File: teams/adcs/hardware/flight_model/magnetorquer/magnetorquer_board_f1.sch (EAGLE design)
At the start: 35 parts, among them U5 LTC3624

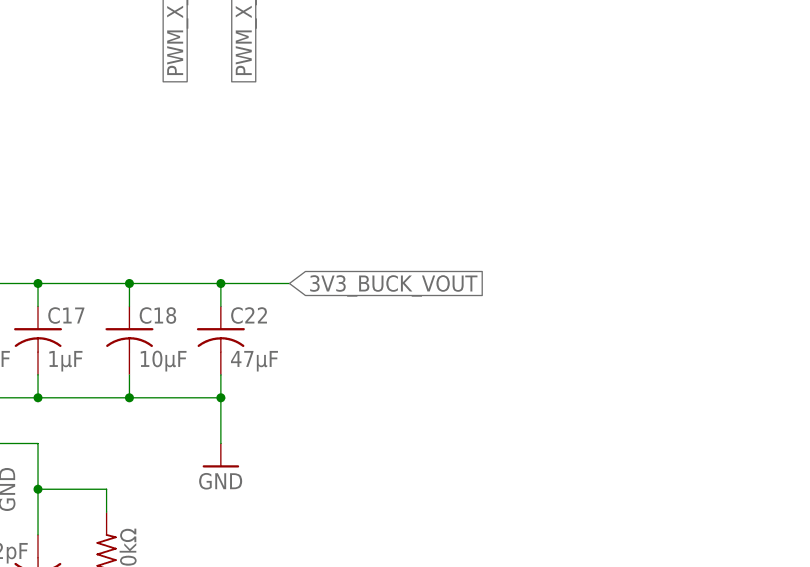
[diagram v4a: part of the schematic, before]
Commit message: ADCS/MT: Properly connect buck converter and reposition smoothing capacitors on H-Bridge
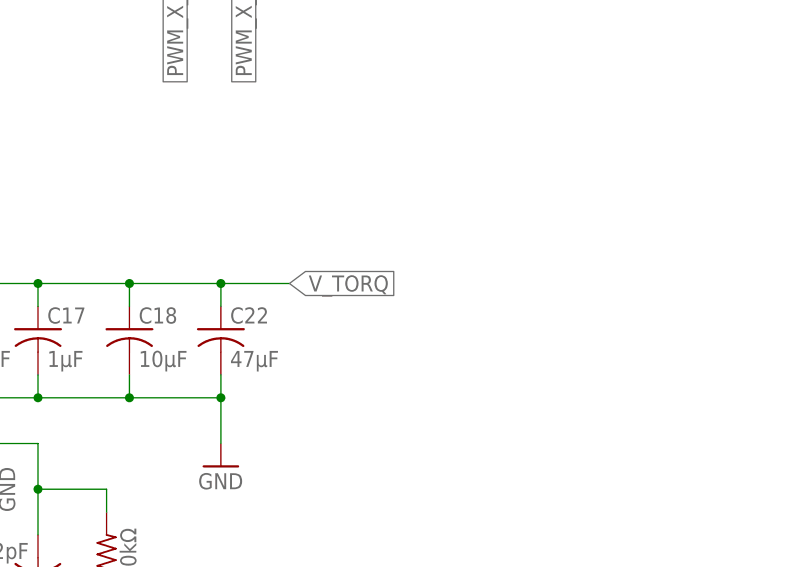
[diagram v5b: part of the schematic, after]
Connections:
- removed net 3V3_BUCK_VOUT: C15.2, C16.1, C17.1, C18.1, C22.1, L2.P$2, R6.2
- net V_TORQ: now also C15.2, C16.1, C17.1, C18.1, C22.1, L2.P$2, R6.2
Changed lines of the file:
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@@
 <label x="337.82" y="81.28" size="1.778" layer="95" xref="yes"/>
+</segment>
+<segment>
+<pinref part="L2" gate="G$1" pin="P$2"/>
+<wire x1="205.74" y1="-7.62" x2="215.9" y2="-7.62" width="0.1524" layer="91"/>
+<pinref part="R6" gate="G$1" pin="2"/>
+<wire x1="215.9" y1="-7.62" x2="220.98" y2="-7.62" width="0.1524" layer="91"/>
+<wire x1="220.98" y1="-7.62" x2="231.14" y2="-7.62" width="0.1524" layer="91"/>
+<wire x1="231.14" y1="-7.62" x2="241.3" y2="-7.62" width="0.1524" layer="91"/>
+<wire x1="241.3" y1="-7.62" x2="251.46" y2="-7.62" width="0.1524" layer="91"/>
+<wire x1="231.14" y1="-25.4" x2="231.14" y2="-30.48" width="0.1524" layer="91"/>
+<wire x1="231.14" y1="-30.48" x2="238.76" y2="-30.48" width="0.1524" layer="91"/>
+<wire x1="238.76" y1="-30.48" x2="238.76" y2="-33.02" width="0.1524" layer="91"/>
+<pinref part="C15" gate="G$1" pin="2"/>
+<wire x1="231.14" y1="-35.56" x2="231.14" y2="-30.48" width="0.1524" layer="91"/>
+<junction x="231.14" y="-30.48"/>
+<wire x1="231.14" y1="-25.4" x2="215.9" y2="-25.4" width="0.1524" layer="91"/>
+<wire x1="215.9" y1="-25.4" x2="215.9" y2="-7.62" width="0.1524" layer="91"/>
+<junction x="215.9" y="-7.62"/>
+<pinref part="C16" gate="G$1" pin="1"/>
+<wire x1="220.98" y1="-10.16" x2="220.98" y2="-7.62" width="0.1524" layer="91"/>
+<junction x="220.98" y="-7.62"/>
+<pinref part="C17" gate="G$1" pin="1"/>
+<wire x1="231.14" y1="-10.16" x2="231.14" y2="-7.62" width="0.1524" layer="91"/>
+<junction x="231.14" y="-7.62"/>
+<pinref part="C18" gate="G$1" pin="1"/>
+<wire x1="241.3" y1="-10.16" x2="241.3" y2="-7.62" width="0.1524" layer="91"/>
+<junction x="241.3" y="-7.62"/>
+<pinref part="C22" gate="G$1" pin="1"/>
+<wire x1="251.46" y1="-10.16" x2="251.46" y2="-7.62" width="0.1524" layer="91"/>
+<wire x1="251.46" y1="-7.62" x2="259.08" y2="-7.62" width="0.1524" layer="91"/>
+<junction x="251.46" y="-7.62"/>
+<label x="259.08" y="-7.62" size="1.778" layer="95" xref="yes"/>
 </segment>
 </net>
@@
 </segment>
 </net>
-<net name="3V3_BUCK_VOUT" class="0">
-<segment>
-<pinref part="L2" gate="G$1" pin="P$2"/>
-<wire x1="205.74" y1="-7.62" x2="215.9" y2="-7.62" width="0.1524" layer="91"/>
-<pinref part="R6" gate="G$1" pin="2"/>
-<wire x1="215.9" y1="-7.62" x2="220.98" y2="-7.62" width="0.1524" layer="91"/>
-<wire x1="220.98" y1="-7.62" x2="231.14" y2="-7.62" width="0.1524" layer="91"/>
-<wire x1="231.14" y1="-7.62" x2="241.3" y2="-7.62" width="0.1524" layer="91"/>
-<wire x1="241.3" y1="-7.62" x2="251.46" y2="-7.62" width="0.1524" layer="91"/>
-<wire x1="231.14" y1="-25.4" x2="231.14" y2="-30.48" width="0.1524" layer="91"/>
-<wire x1="231.14" y1="-30.48" x2="238.76" y2="-30.48" width="0.1524" layer="91"/>
-<wire x1="238.76" y1="-30.48" x2="238.76" y2="-33.02" width="0.1524" layer="91"/>
-<pinref part="C15" gate="G$1" pin="2"/>
-<wire x1="231.14" y1="-35.56" x2="231.14" y2="-30.48" width="0.1524" layer="91"/>
-<junction x="231.14" y="-30.48"/>
-<wire x1="231.14" y1="-25.4" x2="215.9" y2="-25.4" width="0.1524" layer="91"/>
-<wire x1="215.9" y1="-25.4" x2="215.9" y2="-7.62" width="0.1524" layer="91"/>
-<junction x="215.9" y="-7.62"/>
-<pinref part="C16" gate="G$1" pin="1"/>
-<wire x1="220.98" y1="-10.16" x2="220.98" y2="-7.62" width="0.1524" layer="91"/>
-<junction x="220.98" y="-7.62"/>
-<pinref part="C17" gate="G$1" pin="1"/>
-<wire x1="231.14" y1="-10.16" x2="231.14" y2="-7.62" width="0.1524" layer="91"/>
-<junction x="231.14" y="-7.62"/>
-<pinref part="C18" gate="G$1" pin="1"/>
-<wire x1="241.3" y1="-10.16" x2="241.3" y2="-7.62" width="0.1524" layer="91"/>
-<junction x="241.3" y="-7.62"/>
-<pinref part="C22" gate="G$1" pin="1"/>
-<wire x1="251.46" y1="-10.16" x2="251.46" y2="-7.62" width="0.1524" layer="91"/>
-<wire x1="251.46" y1="-7.62" x2="259.08" y2="-7.62" width="0.1524" layer="91"/>
-<junction x="251.46" y="-7.62"/>
-<label x="259.08" y="-7.62" size="1.778" layer="95" xref="yes"/>
-</segment>
-</net>

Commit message: PC104 connector change: switched X and Y pin assignments, MQT board: converted to 4 layer board, layer 4 GND, previous layer 2 traces moved to new layer 2; added X and Y MQT outputs; added 3x LDOs
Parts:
- added .C1, .C13, .C15, .C6, .C7, .C9: 4.7u, SparkFun-Capacitors:CAP1206
- added .C14, .C5, .C8: 10n, SparkFun-Capacitors:CAP0805
- added C1, C2, C3: 1uF, DubSat1 Components:CAPACITOR0805
- added R10, R11, R12: 0, DubSat1 Components:RESISTOR0805
- added R13: 0, DubSat1 Components:RESISTOR2010
- added R14: DNP, DubSat1 Components:RESISTOR2010
- added R4, R5, R9: DNP, DubSat1 Components:RESISTOR0805
- added U$4, U$5, U$9: ANALOG_LDO_ADM7172, ICs:ANALOG_LDO_ADM7172
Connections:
- removed net V_TORQ: C15.2, C16.1, C17.1, C18.1, C22.1, C7.2, C8.2, C9.2, L2.P$2, R6.2, U1.VDD, U2.VDD, U3.VDD
- new net N$11: .C8.1, U$5.SS
- new net N$15: .C14.1, U$9.SS
- new net N$9: .C5.1, U$4.SS
- new net VBUCK: C15.2, C16.1, C17.1, C18.1, C22.1, L2.P$2, R13.1, R6.2
- new net VBUCK/VBAT: .C1.1, .C13.1, .C7.1, R10.1, R11.1, R12.1, R13.2, R14.2, U$4.EN, U$4.VIN1, U$4.VIN2, U$5.EN, U$5.VIN1, U$5.VIN2, U$9.EN, U$9.VIN1, U$9.VIN2
- new net VOUT-X: .C9.1, R4.1, U$5.SENSE, U$5.VOUT1, U$5.VOUT2
- new net VOUT-Y: .C15.1, R5.1, U$9.SENSE, U$9.VOUT1, U$9.VOUT2
- new net VOUT-Z: .C6.1, R9.1, U$4.SENSE, U$4.VOUT1, U$4.VOUT2
- new net V_TORQ-X: C1.2, C8.2, R11.2, R4.2, U2.VDD
- new net V_TORQ-Y: C2.2, C7.2, R12.2, R5.2, U1.VDD
- new net V_TORQ-Z: C3.2, C9.2, R10.2, R9.2, U3.VDD
- net GND: now also .C1.2, .C13.2, .C14.2, .C15.2, .C5.2, .C6.2, .C7.2, .C8.2, .C9.2, C1.1, C2.1, C3.1, U$4.GND, U$4.GNDP, U$5.GND, U$5.GNDP, U$9.GND, U$9.GNDP
- net MT_X_A: now also U$1.MT_X_A@39, U$1.MT_X_A@40; no longer U$1.MT_X_A@1, U$1.MT_X_A@2
- net MT_X_B: now also U$1.MT_X_B@43, U$1.MT_X_B@44; no longer U$1.MT_X_B@1, U$1.MT_X_B@2
- net MT_Y_A: now also U$1.MT_Y_A@37, U$1.MT_Y_A@38; no longer U$1.MT_Y_A@1, U$1.MT_Y_A@2
- net MT_Y_B: now also U$1.MT_Y_B@41, U$1.MT_Y_B@42; no longer U$1.MT_Y_B@1, U$1.MT_Y_B@2
- net VBAT: now also R14.1
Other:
- note added: "selects net for large current carrying trace"
- moved on the sheet: C7, C8, C9, R1, R2, R3

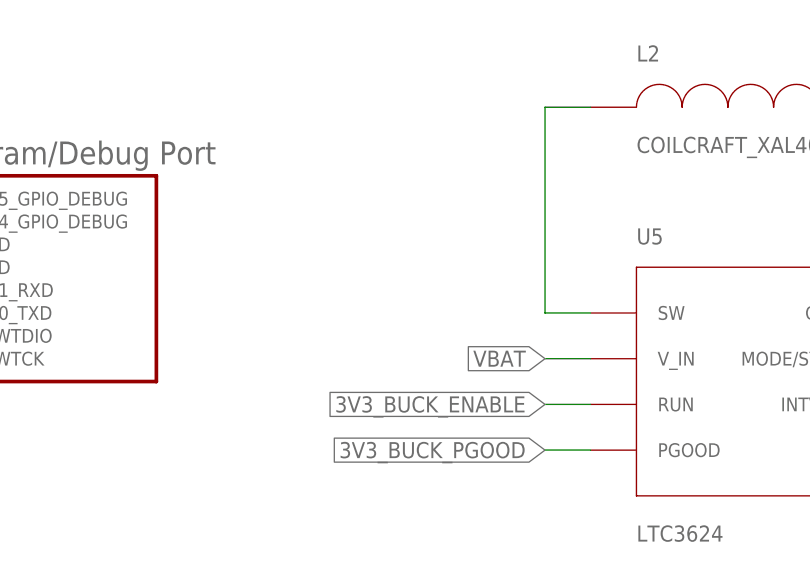
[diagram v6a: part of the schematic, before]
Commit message: ADCS/MT: Add input capacitance on buck converter
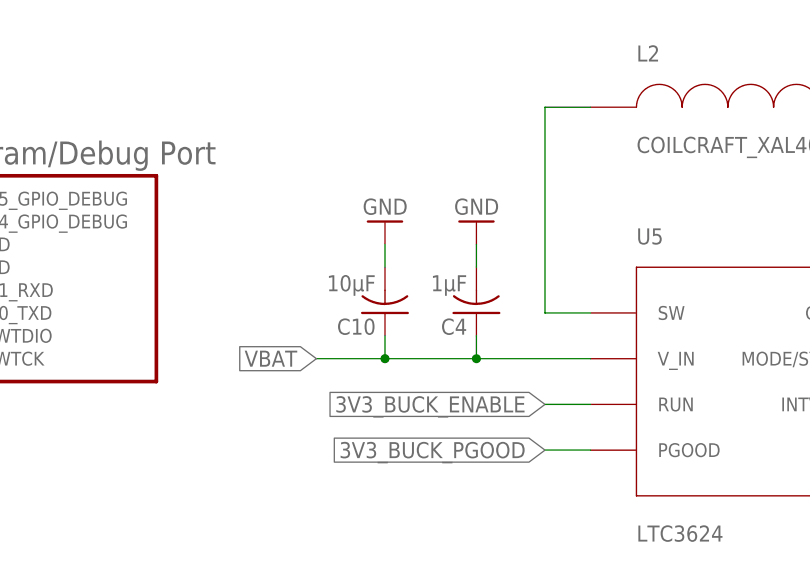
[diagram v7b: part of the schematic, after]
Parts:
- added C10: 10µF, rcl:C-USC0805
- added C4: 1µF, rcl:C-USC0805
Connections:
- net GND: now also C10.2, C4.2
- net VBAT: now also C10.1, C4.1
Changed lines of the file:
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@@
 <?xml version="1.0" encoding="utf-8"?>
 <!DOCTYPE eagle SYSTEM "eagle.dtd">
-<eagle version="8.4.2">
+<eagle version="9.0.0">
 <drawing>
 <settings>
@@
 <part name="R13" library="DubSat1 Components" deviceset="RESISTOR" device="2010" value="0"/>
 <part name="R14" library="DubSat1 Components" deviceset="RESISTOR" device="2010" value="DNP"/>
+<part name="C4" library="rcl" library_urn="urn:adsk.eagle:library:334" deviceset="C-US" device="C0805" package3d_urn="urn:adsk.eagle:package:23617/2" value="1µF"/>
+<part name="C10" library="rcl" library_urn="urn:adsk.eagle:library:334" deviceset="C-US" device="C0805" package3d_urn="urn:adsk.eagle:package:23617/2" value="10µF"/>
+<part name="GND10" library="supply1" library_urn="urn:adsk.eagle:library:371" deviceset="GND" device=""/>
+<part name="GND14" library="supply1" library_urn="urn:adsk.eagle:library:371" deviceset="GND" device=""/>
 </parts>
 <sheets>
@@
 <instance part="R13" gate="G$1" x="101.6" y="114.3"/>
 <instance part="R14" gate="G$1" x="101.6" y="124.46"/>
+<instance part="C4" gate="G$1" x="162.56" y="-30.48" rot="R180"/>
+<instance part="C10" gate="G$1" x="152.4" y="-30.48" rot="R180"/>
+<instance part="GND10" gate="1" x="152.4" y="-20.32" rot="R180"/>
+<instance part="GND14" gate="1" x="162.56" y="-20.32" rot="R180"/>
 </instances>
 <busses>
@@
 <wire x1="198.12" y1="137.16" x2="198.12" y2="139.7" width="0.1524" layer="91"/>
 </segment>
+<segment>
+<pinref part="C10" gate="G$1" pin="2"/>
+<pinref part="GND10" gate="1" pin="GND"/>
+<wire x1="152.4" y1="-25.4" x2="152.4" y2="-22.86" width="0.1524" layer="91"/>
+</segment>
+<segment>
+<pinref part="C4" gate="G$1" pin="2"/>
+<pinref part="GND14" gate="1" pin="GND"/>
+<wire x1="162.56" y1="-25.4" x2="162.56" y2="-22.86" width="0.1524" layer="91"/>
+</segment>
 </net>
 <net name="PWM_X_1" class="0">
@@
 <segment>
 <pinref part="U5" gate="G$1" pin="V_IN"/>
-<wire x1="175.26" y1="-35.56" x2="170.18" y2="-35.56" width="0.1524" layer="91"/>
-<label x="170.18" y="-35.56" size="1.778" layer="95" rot="R180" xref="yes"/>
-</segment>
-<segment>
+<wire x1="175.26" y1="-35.56" x2="162.56" y2="-35.56" width="0.1524" layer="91"/>
+<label x="144.78" y="-35.56" size="1.778" layer="95" rot="R180" xref="yes"/>
+<pinref part="C10" gate="G$1" pin="1"/>
+<wire x1="162.56" y1="-35.56" x2="152.4" y2="-35.56" width="0.1524" layer="91"/>
+<wire x1="152.4" y1="-35.56" x2="144.78" y2="-35.56" width="0.1524" layer="91"/>
+<wire x1="152.4" y1="-35.56" x2="152.4" y2="-33.02" width="0.1524" layer="91"/>
+<junction x="152.4" y="-35.56"/>
+<pinref part="C4" gate="G$1" pin="1"/>
+<wire x1="162.56" y1="-35.56" x2="162.56" y2="-33.02" width="0.1524" layer="91"/>
+<junction x="162.56" y="-35.56"/>
+</segment>
+<segment>

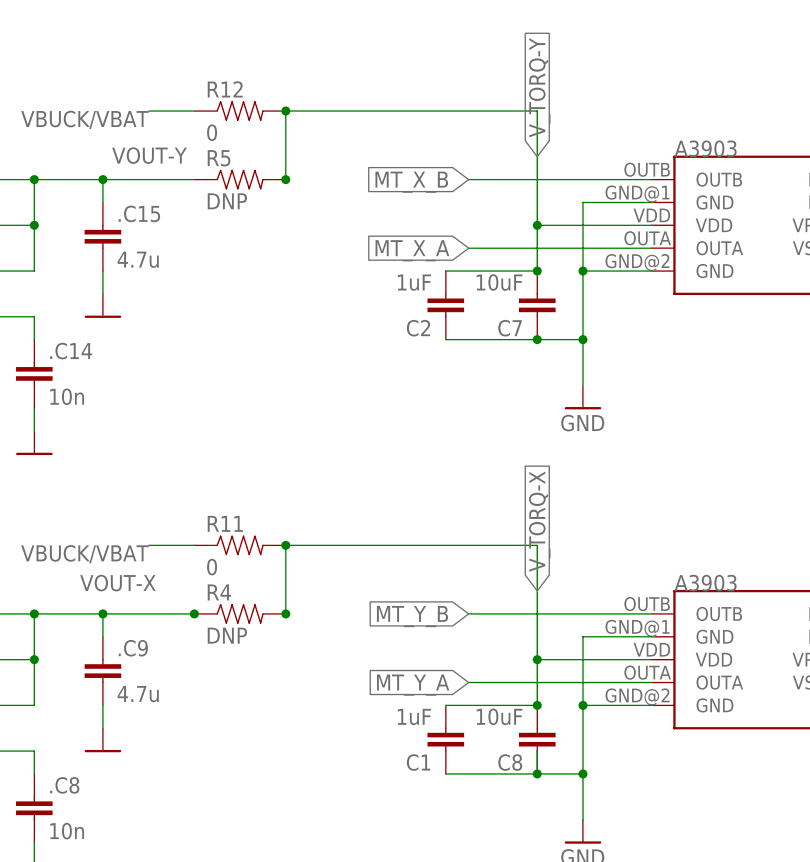
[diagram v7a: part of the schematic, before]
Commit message: ADCS/MT: Fix magnetorquer current output coils
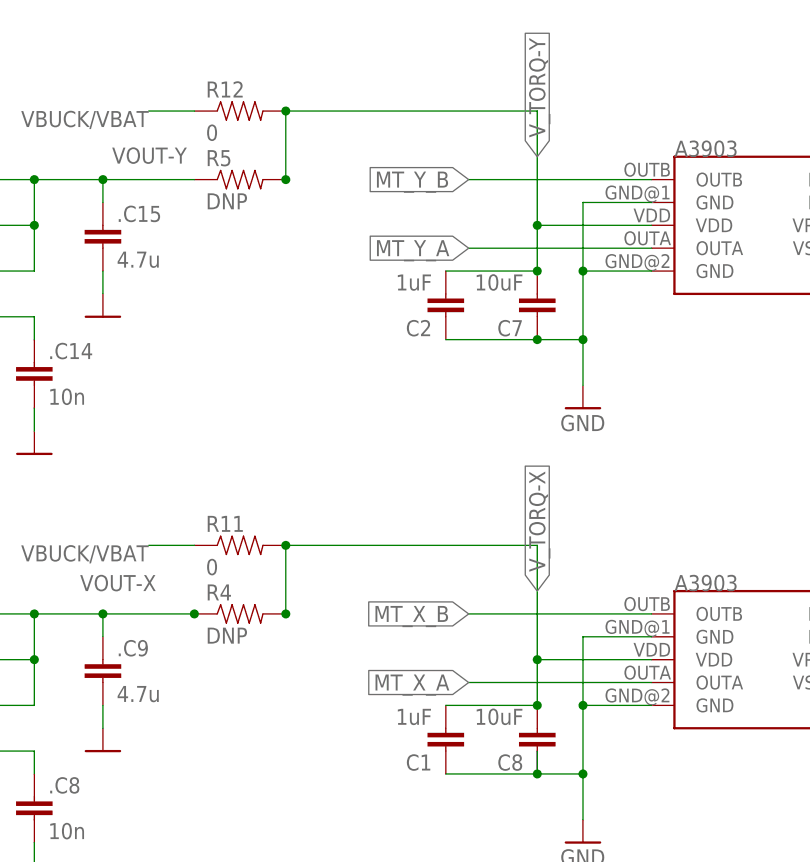
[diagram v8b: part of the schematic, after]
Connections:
- net MT_X_A: now also U2.OUTA; no longer U1.OUTA
- net MT_X_B: now also U2.OUTB; no longer U1.OUTB
- net MT_Y_A: now also U1.OUTA; no longer U2.OUTA
- net MT_Y_B: now also U1.OUTB; no longer U2.OUTB
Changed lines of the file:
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@@
 <net name="MT_X_B" class="0">
-<segment>
-<pinref part="U1" gate="G$1" pin="OUTB"/>
-<wire x1="259.08" y1="149.86" x2="238.76" y2="149.86" width="0.1524" layer="91"/>
-<label x="238.76" y="149.86" size="1.778" layer="95" rot="R180" xref="yes"/>
-</segment>
 <segment>
 <wire x1="48.26" y1="60.96" x2="48.26" y2="58.42" width="0.1524" layer="91"/>
@@
 <label x="114.3" y="58.42" size="1.778" layer="95" rot="R270" xref="yes"/>
 </segment>
+<segment>
+<pinref part="U2" gate="G$1" pin="OUTB"/>
+<wire x1="259.08" y1="101.6" x2="238.76" y2="101.6" width="0.1524" layer="91"/>
+<label x="238.76" y="101.6" size="1.778" layer="95" rot="R180" xref="yes"/>
+</segment>
 </net>
 <net name="MT_X_A" class="0">
-<segment>
-<pinref part="U1" gate="G$1" pin="OUTA"/>
-<wire x1="259.08" y1="142.24" x2="238.76" y2="142.24" width="0.1524" layer="91"/>
-<label x="238.76" y="142.24" size="1.778" layer="95" rot="R180" xref="yes"/>
-</segment>
 <segment>
 <pinref part="U$1" gate="G$1" pin="MT_X_A@39"/>
@@
 <pinref part="U$1" gate="G$1" pin="MT_X_A@40"/>
 <wire x1="114.3" y1="63.5" x2="106.68" y2="63.5" width="0.1524" layer="91"/>
+</segment>
+<segment>
+<pinref part="U2" gate="G$1" pin="OUTA"/>
+<wire x1="259.08" y1="93.98" x2="238.76" y2="93.98" width="0.1524" layer="91"/>
+<label x="238.76" y="93.98" size="1.778" layer="95" rot="R180" xref="yes"/>
 </segment>
 </net>
@@
 <net name="MT_Y_A" class="0">
 <segment>
-<pinref part="U2" gate="G$1" pin="OUTA"/>
-<wire x1="259.08" y1="93.98" x2="238.76" y2="93.98" width="0.1524" layer="91"/>
-<label x="238.76" y="93.98" size="1.778" layer="95" rot="R180" xref="yes"/>
-</segment>
-<segment>
 <pinref part="U$1" gate="G$1" pin="MT_Y_A@37"/>
 <wire x1="-22.86" y1="63.5" x2="-27.94" y2="63.5" width="0.1524" layer="91"/>
@@
 <wire x1="38.1" y1="63.5" x2="30.48" y2="63.5" width="0.1524" layer="91"/>
 </segment>
+<segment>
+<pinref part="U1" gate="G$1" pin="OUTA"/>
+<wire x1="259.08" y1="142.24" x2="238.76" y2="142.24" width="0.1524" layer="91"/>
+<label x="238.76" y="142.24" size="1.778" layer="95" rot="R180" xref="yes"/>
+</segment>
 </net>
 <net name="MT_Y_B" class="0">
-<segment>
-<pinref part="U2" gate="G$1" pin="OUTB"/>
-<wire x1="259.08" y1="101.6" x2="238.76" y2="101.6" width="0.1524" layer="91"/>
-<label x="238.76" y="101.6" size="1.778" layer="95" rot="R180" xref="yes"/>
-</segment>
 <segment>
 <wire x1="-30.48" y1="60.96" x2="-30.48" y2="68.58" width="0.1524" layer="91"/>
@@
 <label x="38.1" y="58.42" size="1.778" layer="95" rot="R270" xref="yes"/>
 </segment>
-</net>
+<segment>
+<pinref part="U1" gate="G$1" pin="OUTB"/>
+<wire x1="259.08" y1="149.86" x2="238.76" y2="149.86" width="0.1524" layer="91"/>
+<label x="238.76" y="149.86" size="1.778" layer="95" rot="R180" xref="yes"/>
+</segment>
+</net>
